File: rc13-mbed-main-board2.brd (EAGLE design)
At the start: 130 x 100 mm, 44 parts, among them IC1 MBED_MICROCONTROLLER, U1 PCA9555PW,118, X1 BALL_SENS, X2 ETH, X5 BTNS, X9 COIL

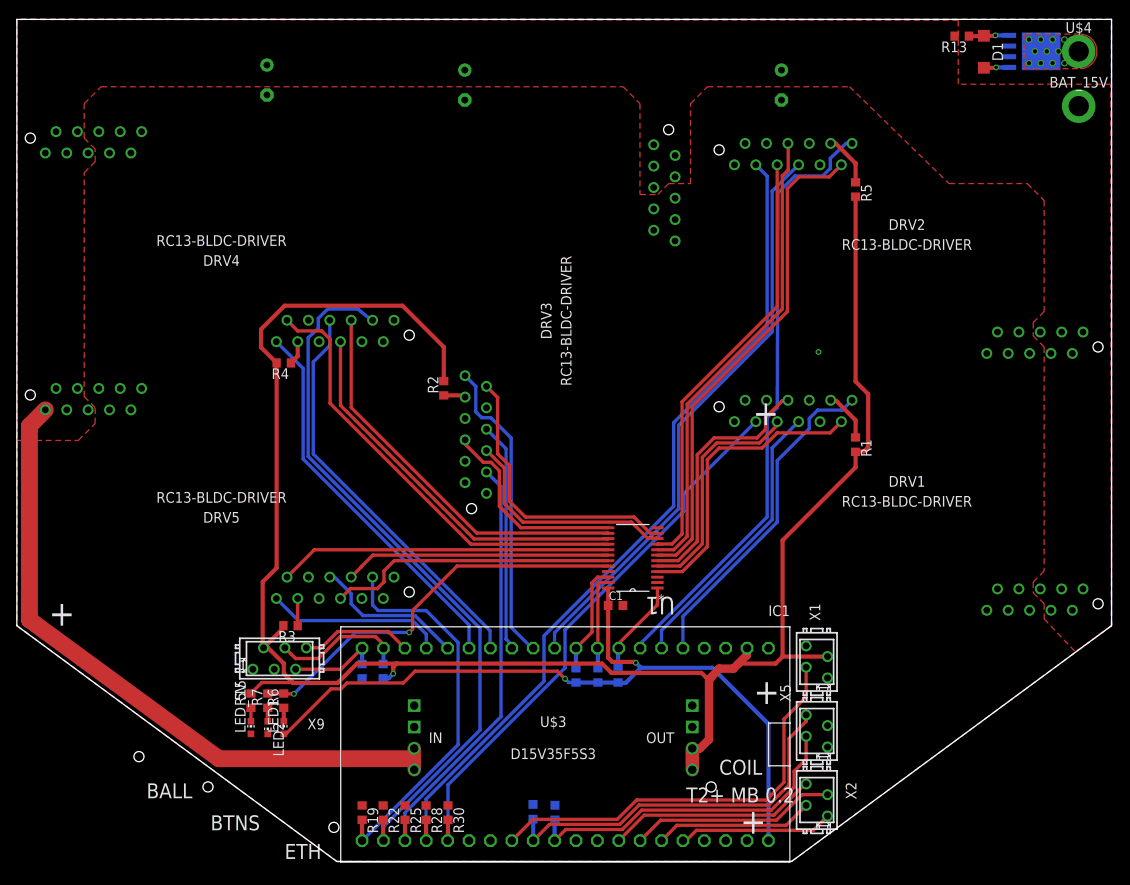
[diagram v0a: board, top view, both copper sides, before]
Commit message: Improved routing
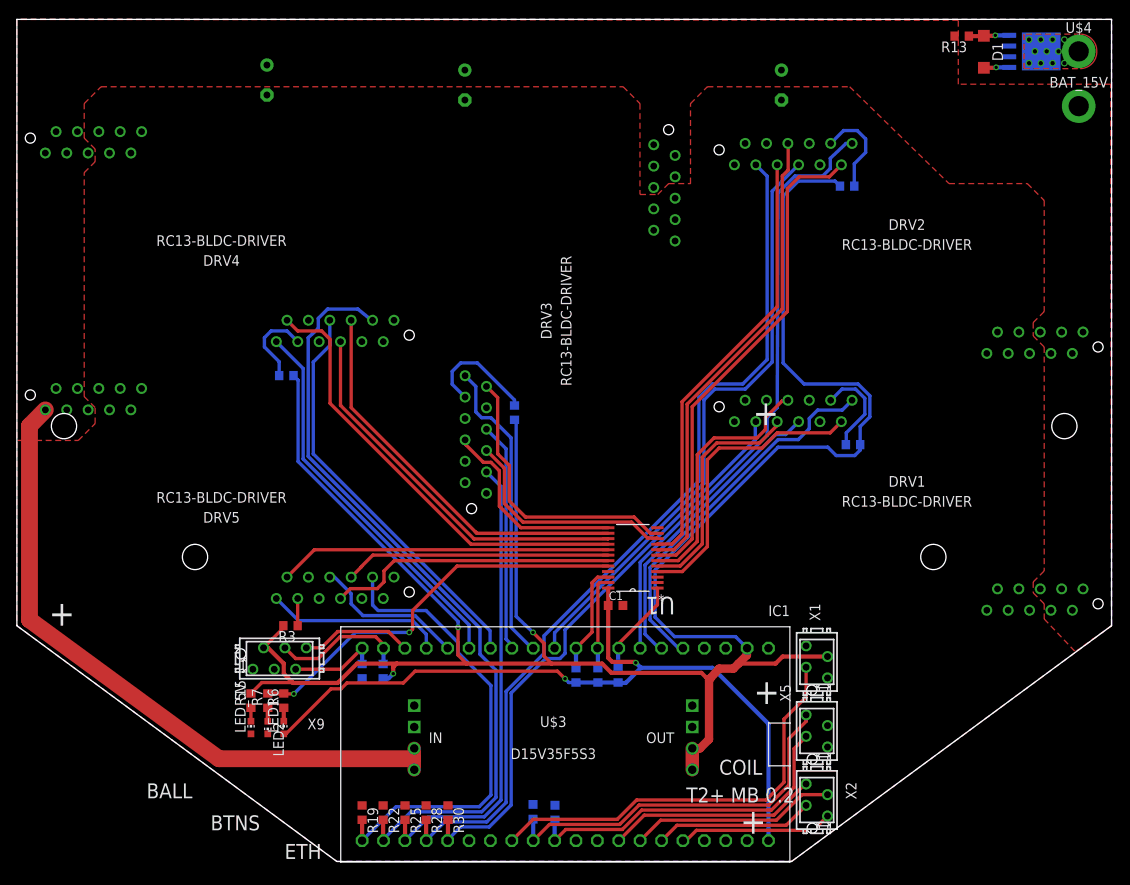
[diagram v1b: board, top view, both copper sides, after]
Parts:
- moved R2 8.89 mm to (59.1, 53.3), flipped to the bottom, turned to 270 degrees
- moved R4 1.53 mm to (32.0, 57.7), flipped to the bottom
- moved R5 1.08 mm to (98.6, 80.2), flipped to the bottom, turned to 0 degrees
- moved R1 0.30 mm to (99.3, 49.5), flipped to the bottom, turned to 180 degrees
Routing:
- net +5V: track 227.5 -> 268.0 mm, vias 1 -> 3
- net N$6: track 2.61 -> 14.0 mm
- net PWM5: track 46.0 -> 55.1 mm
- net N$4: track 2.86 -> 10.0 mm
- net PWM4: track 85.6 -> 92.1 mm
- net N$2: track 5.99 -> 11.5 mm
- net N$3: track 6.19 -> 11.4 mm
- net PWM2: track 100.1 -> 105.1 mm
- net DIRO1: track 39.5 -> 44.4 mm
- net PWM3: track 51.7 -> 55.6 mm
- net PWM1: track 67.4 -> 70.4 mm
- net TACHO1: track 33.6 -> 36.1 mm
- net TACHO2: track 69.4 -> 71.5 mm
- net GND: vias 2 -> 1

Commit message: Few small changes
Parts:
- added C3: 470uF, rcl:E3,5-8
- moved C2 17.8 mm to (71.0, 92.2), flipped to the top
- moved C7 17.3 mm to (47.0, 92.2), flipped to the top
- moved C9 6.20 mm to (97.0, 92.2), flipped to the top
- moved U$3 3.30 mm to (67.0, 14.7)
- moved R3 0.86 mm to (32.0, 28.7), flipped to the bottom, turned to 0 degrees
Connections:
- net +15V: now also C3.+
- net GND: now also C3.-
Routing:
- net +15V: track 79.3 -> 82.6 mm
- net DIRO5: track 21.2 -> 22.9 mm
- net +5V: track 268.0 -> 269.4 mm
- net GND: vias 1 -> 27
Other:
- board text removed: "T2+ MB 0.2"
